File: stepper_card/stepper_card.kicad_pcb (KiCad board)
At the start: 2 copper layers, 38.9 x 80 mm, 15 parts, among them J1 Bus_PCI_Express_x1, J2 Conn_01x04, SW1 SW_DIP_x04, U1 DRV8825PWPR_Stepper_Driver

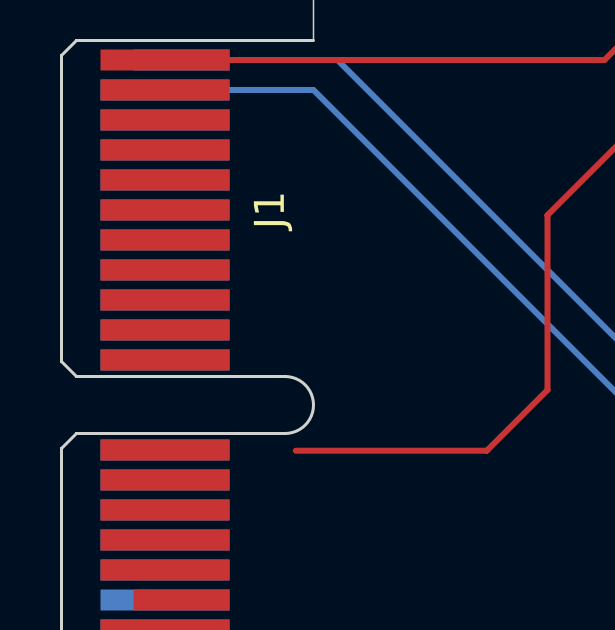
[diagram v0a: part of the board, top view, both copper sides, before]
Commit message: added auto detection trace
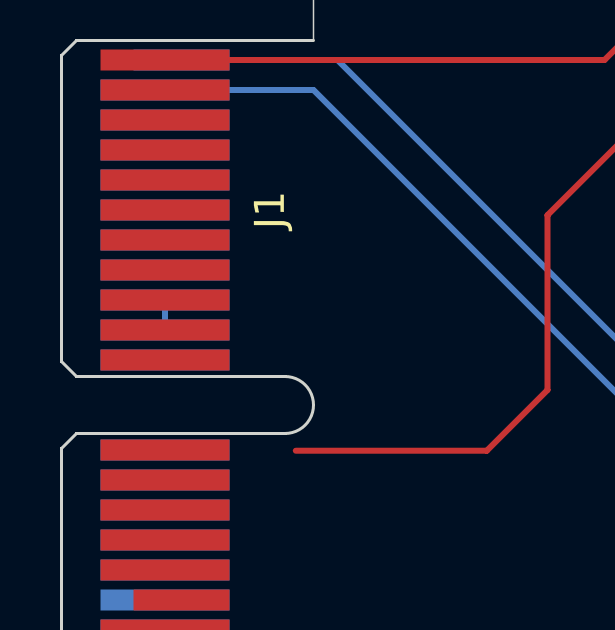
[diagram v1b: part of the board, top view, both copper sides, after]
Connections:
- J1 pad A10: unconnected-(J1-PadA10) -> Net-(J1-PadA10)
- J1 pad A9: unconnected-(J1-PadA9) -> Net-(J1-PadA10)
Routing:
- net Net-(J1-PadA10): track 0.00 -> 1.00 mm

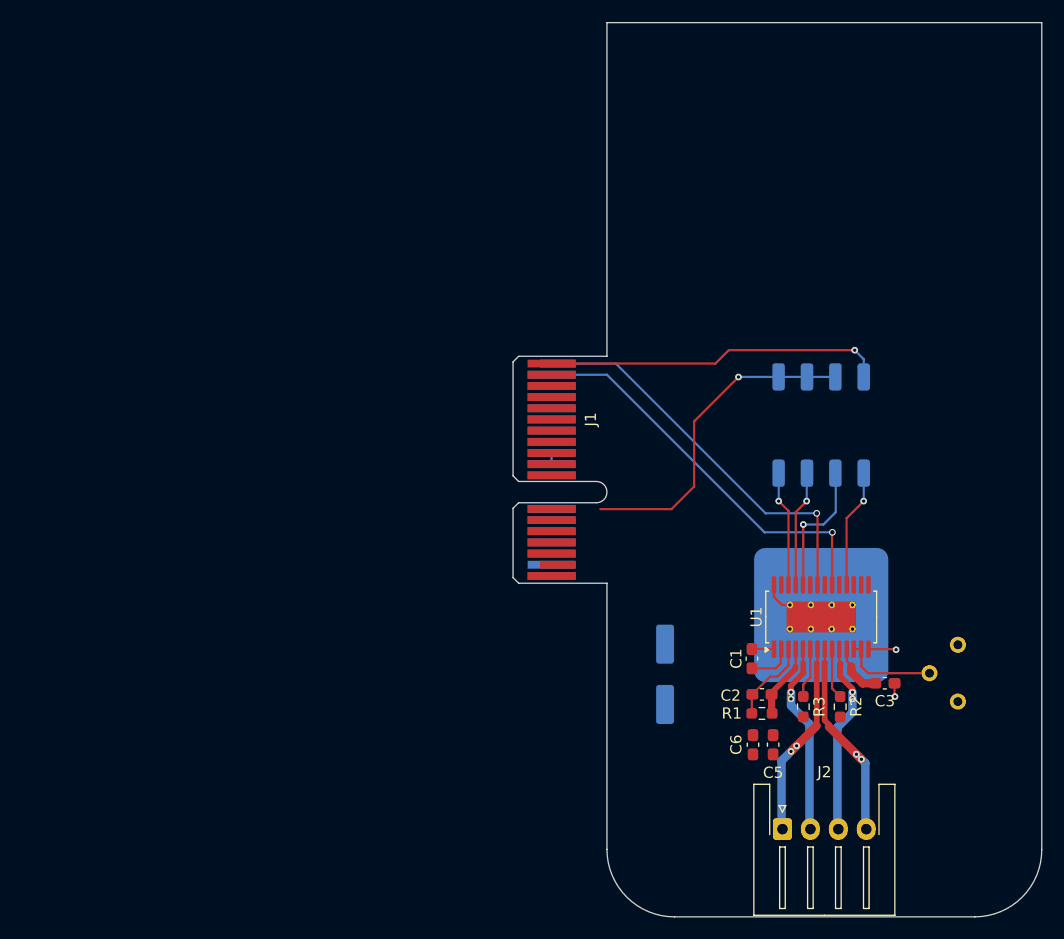
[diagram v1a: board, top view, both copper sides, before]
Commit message: updated layout
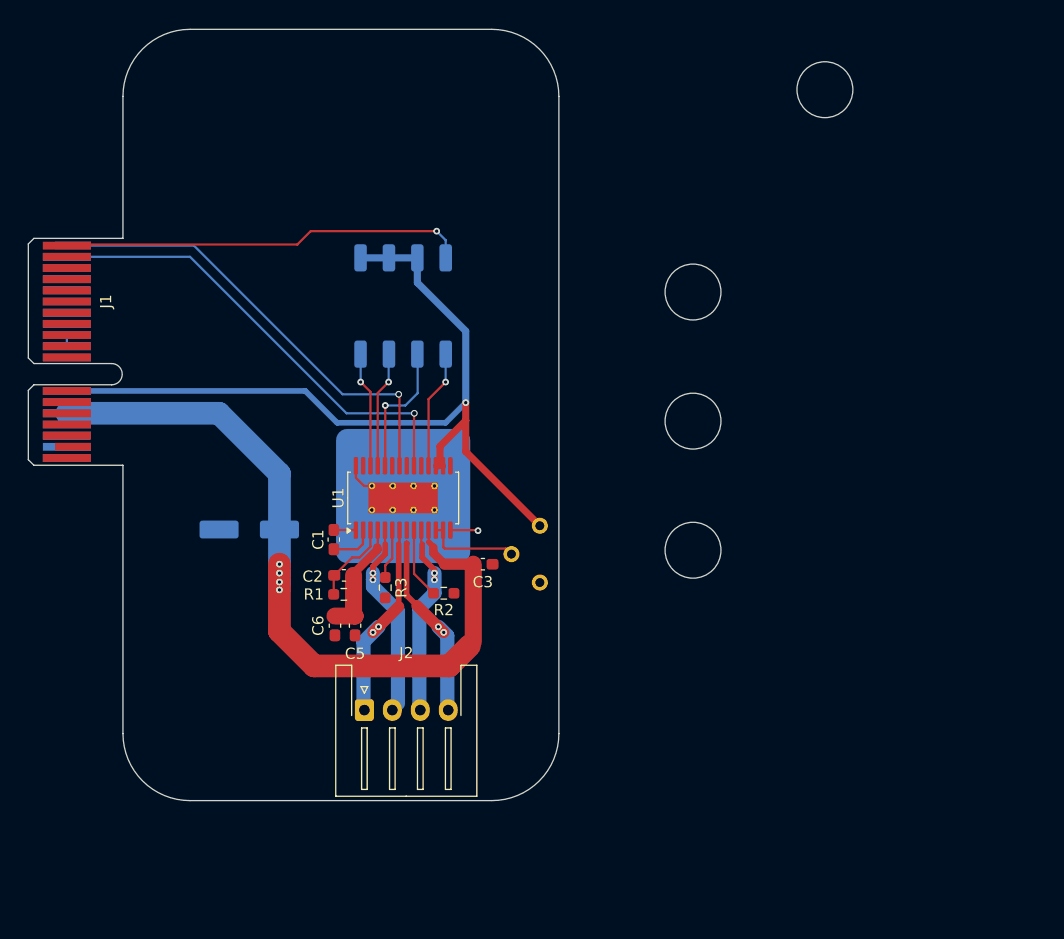
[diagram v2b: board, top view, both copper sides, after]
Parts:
- added H1: MountingHole, MountingHole:MountingHole_5mm, F.Cu at (188.8, 80.9)
- added H2: MountingHole, MountingHole:MountingHole_5mm, F.Cu at (177.0, 99.0)
- added H3: MountingHole, MountingHole:MountingHole_5mm, F.Cu at (177.0, 110.5)
- added H4: MountingHole, MountingHole:MountingHole_5mm, F.Cu at (177.0, 122.1)
- moved J1 44.6 mm to (121.0, 94.8)
- moved C4 39.4 mm to (137.3, 120.2), turned to 180 degrees
- moved C1 38.9 mm to (144.9, 121.2)
- moved C6 38.9 mm to (145.0, 128.8)
- moved HS1 38.9 mm to (151.1, 117.2)
- moved J2 38.9 mm to (147.6, 136.4)
- moved SW1 38.9 mm to (151.1, 100.2)
- moved R3 38.9 mm to (149.5, 125.5)
- moved U1 38.9 mm to (151.1, 117.4)
- moved C2 38.9 mm to (145.8, 124.3)
- moved C5 38.9 mm to (146.8, 128.8)
- moved RV1 38.9 mm to (163.3, 119.9)
- moved R1 38.9 mm to (145.8, 126.0)
- moved C3 37.5 mm to (158.2, 123.3)
- moved R2 36.9 mm to (154.7, 126.0), turned to 0 degrees
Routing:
- net VM: track 11.4 -> 80.7 mm, vias 0 -> 4
- net +3V3: track 29.3 -> 76.8 mm
- net /nFAULT: track 30.3 -> 36.3 mm
- net /STEP: track 35.1 -> 41.1 mm
- net /DIR: track 35.7 -> 41.6 mm
- net /ISB: track 4.54 -> 6.37 mm
- net /B2: track 18.9 -> 17.2 mm
- net GND: track 6.51 -> 5.30 mm, vias 2 -> 1
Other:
- board size 38.9 x 80 mm -> 39.1 x 69 mm

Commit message: finished routing added test points
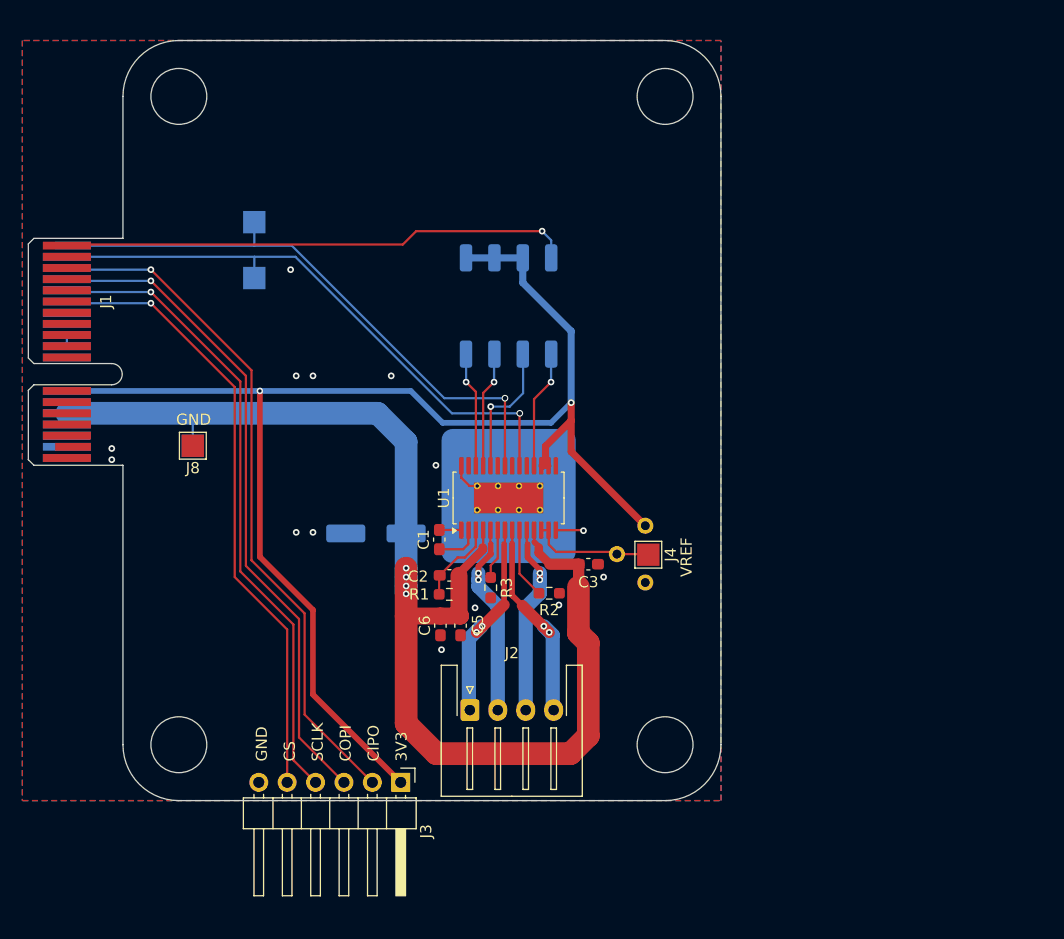
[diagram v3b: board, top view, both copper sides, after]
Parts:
- added J3: Conn_01x06_Pin, Connector_PinHeader_2.54mm:PinHeader_1x06_P2.54mm_Horizontal, F.Cu at (150.8, 142.9)
- added J4: Conn_01x01_Pin, TestPoint:TestPoint_Pad_2.0x2.0mm, F.Cu at (173.0, 122.5)
- added J5: Conn_01x01_Pin, TestPoint:TestPoint_Pad_2.0x2.0mm, B.Cu at (137.8, 97.8)
- added J6: Conn_01x01_Pin, TestPoint:TestPoint_Pad_2.0x2.0mm, B.Cu at (137.8, 92.8)
- added J7: Conn_01x01_Pin, TestPoint:TestPoint_Pad_2.0x2.0mm, B.Cu at (132.2, 112.8)
- added J8: Conn_01x01_Pin, TestPoint:TestPoint_Pad_2.0x2.0mm, F.Cu at (132.2, 112.8)
- moved H3 54.4 mm to (131.0, 139.5)
- moved H2 49.2 mm to (131.0, 81.5)
- moved H4 17.6 mm to (174.5, 139.5)
- moved H1 14.3 mm to (174.5, 81.5)
- moved C4 11.3 mm to (148.6, 120.6)
- moved C1 9.43 mm to (154.3, 121.2)
- moved C3 9.43 mm to (167.6, 123.3)
- moved C6 9.43 mm to (154.4, 128.8)
- moved HS1 9.43 mm to (160.5, 117.2)
- moved J2 9.43 mm to (157.0, 136.4)
- moved R2 9.43 mm to (164.1, 126.0)
- moved R3 9.43 mm to (158.9, 125.5)
- moved SW1 9.43 mm to (160.5, 100.2)
- moved U1 9.43 mm to (160.5, 117.4)
- moved C2 9.43 mm to (155.2, 124.3)
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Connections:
- net Net-(U1-AVREF) renamed /VREF
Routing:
- net /CIPO: track 0.00 -> 61.6 mm, vias 0 -> 1
- net /COPI: track 0.00 -> 59.6 mm, vias 0 -> 1
- net /SCLK: track 0.00 -> 57.5 mm, vias 0 -> 1
- net /CS: track 0.00 -> 55.5 mm, vias 0 -> 1
- net +3V3: track 76.8 -> 126.4 mm, vias 1 -> 2
- net VM: track 80.7 -> 115.3 mm
- net /STEP: track 41.1 -> 52.4 mm
- net /DIR: track 41.6 -> 52.9 mm
- net /nFAULT: track 36.3 -> 45.8 mm
- net /VREF: track 8.55 -> 11.2 mm
- net /B2: track 17.2 -> 18.4 mm
- net GND: vias 1 -> 14
- added copper zone on B.Cu, net GND
- added copper zone on F.Cu, net GND
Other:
- board size 39.1 x 69 mm -> 53.6 x 68 mm
- board text added: "0"
- board text added: "1"
- board text added: "3V3"
- board text added: "CIPO"
- board text added: "COPI"
- board text added: "CS"
- board text added: "DIR"
- board text added: "FAULT"
- board text added: "GND"
- board text added: "MODE0"
- board text added: "MODE1"
- board text added: "MODE2"
- board text added: "ON"
- board text added: "SCLK"
- board text added: "STEP"
- board text added: "VM"
- board text added: "VREF"
